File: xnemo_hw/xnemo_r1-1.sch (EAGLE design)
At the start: 36 parts, among them J1 MICRO_USB_B_RECEPT, J2 DM3D_MICRO_SD, J3 HEADER_2X5_0.05_SMD, J4 HEADER_2X5_0.05_THRU, J5 HEADER_2X5_0.05_THRU, U1 LTC3559, U2 L3GD20, U3 STM32F405RG, U5 HMC5883L, U6 ADXL345, X1 TXC_7A_XTAL

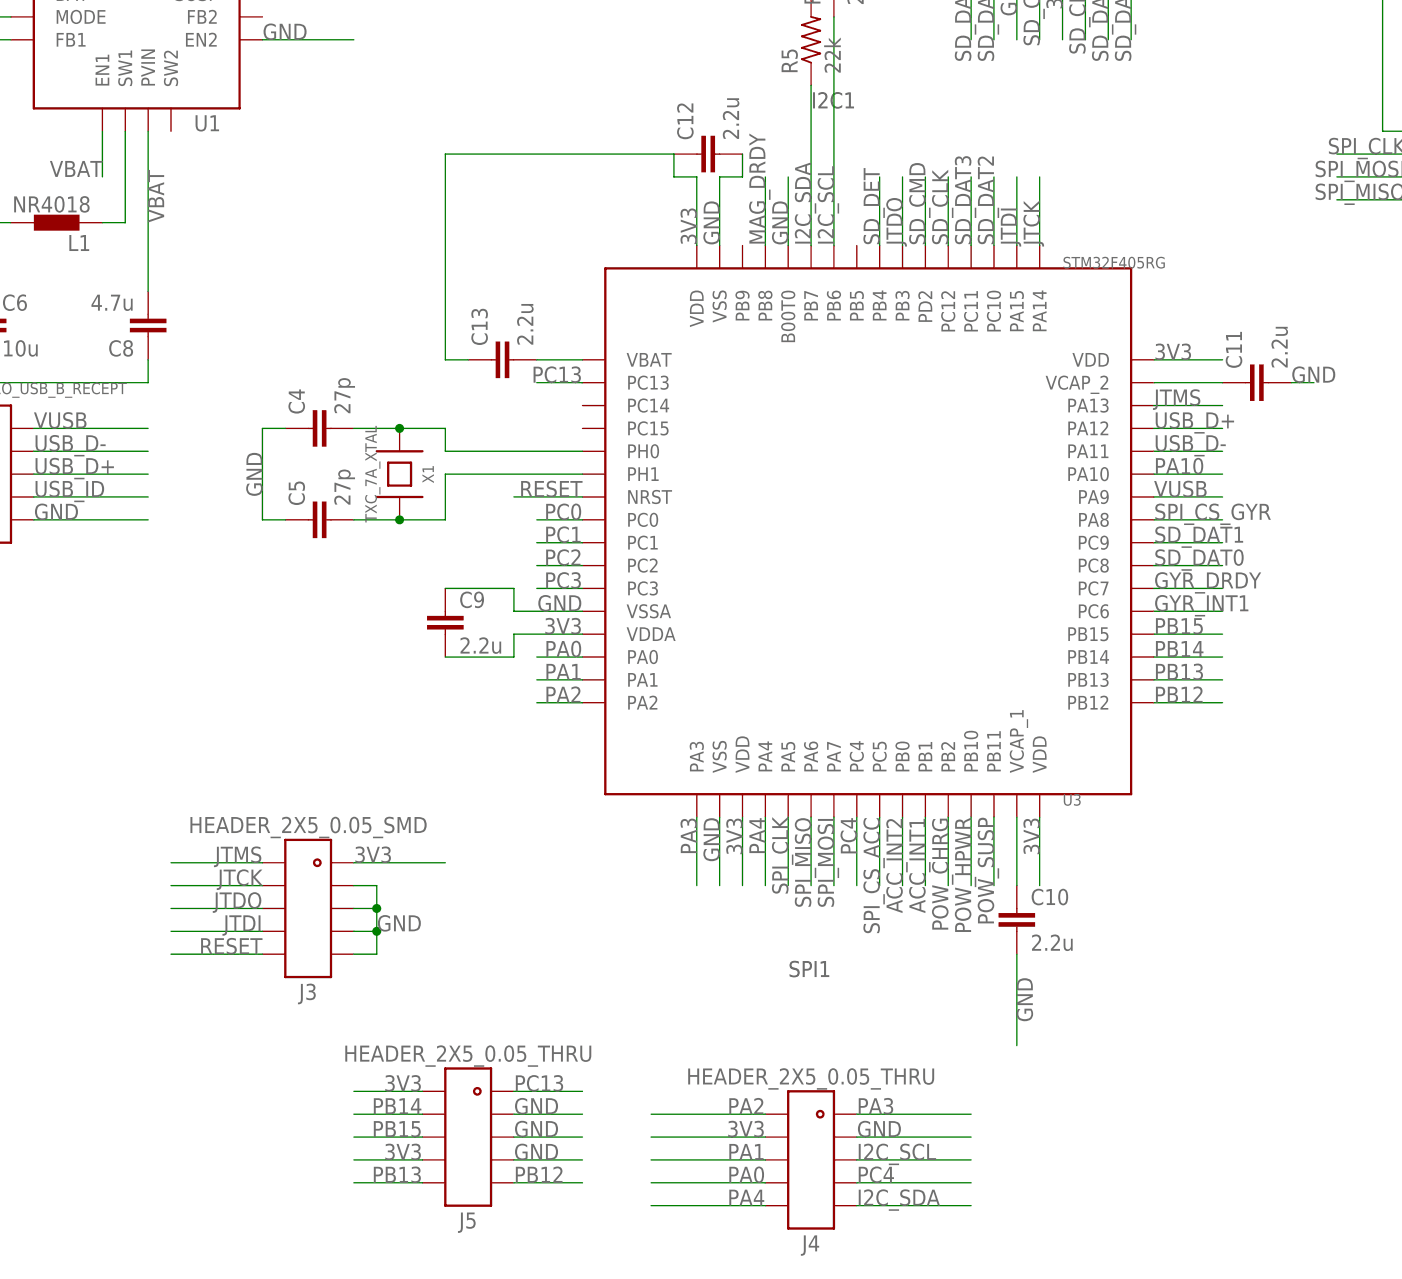
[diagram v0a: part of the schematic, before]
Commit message: Fixing up R1 schematic for R1A
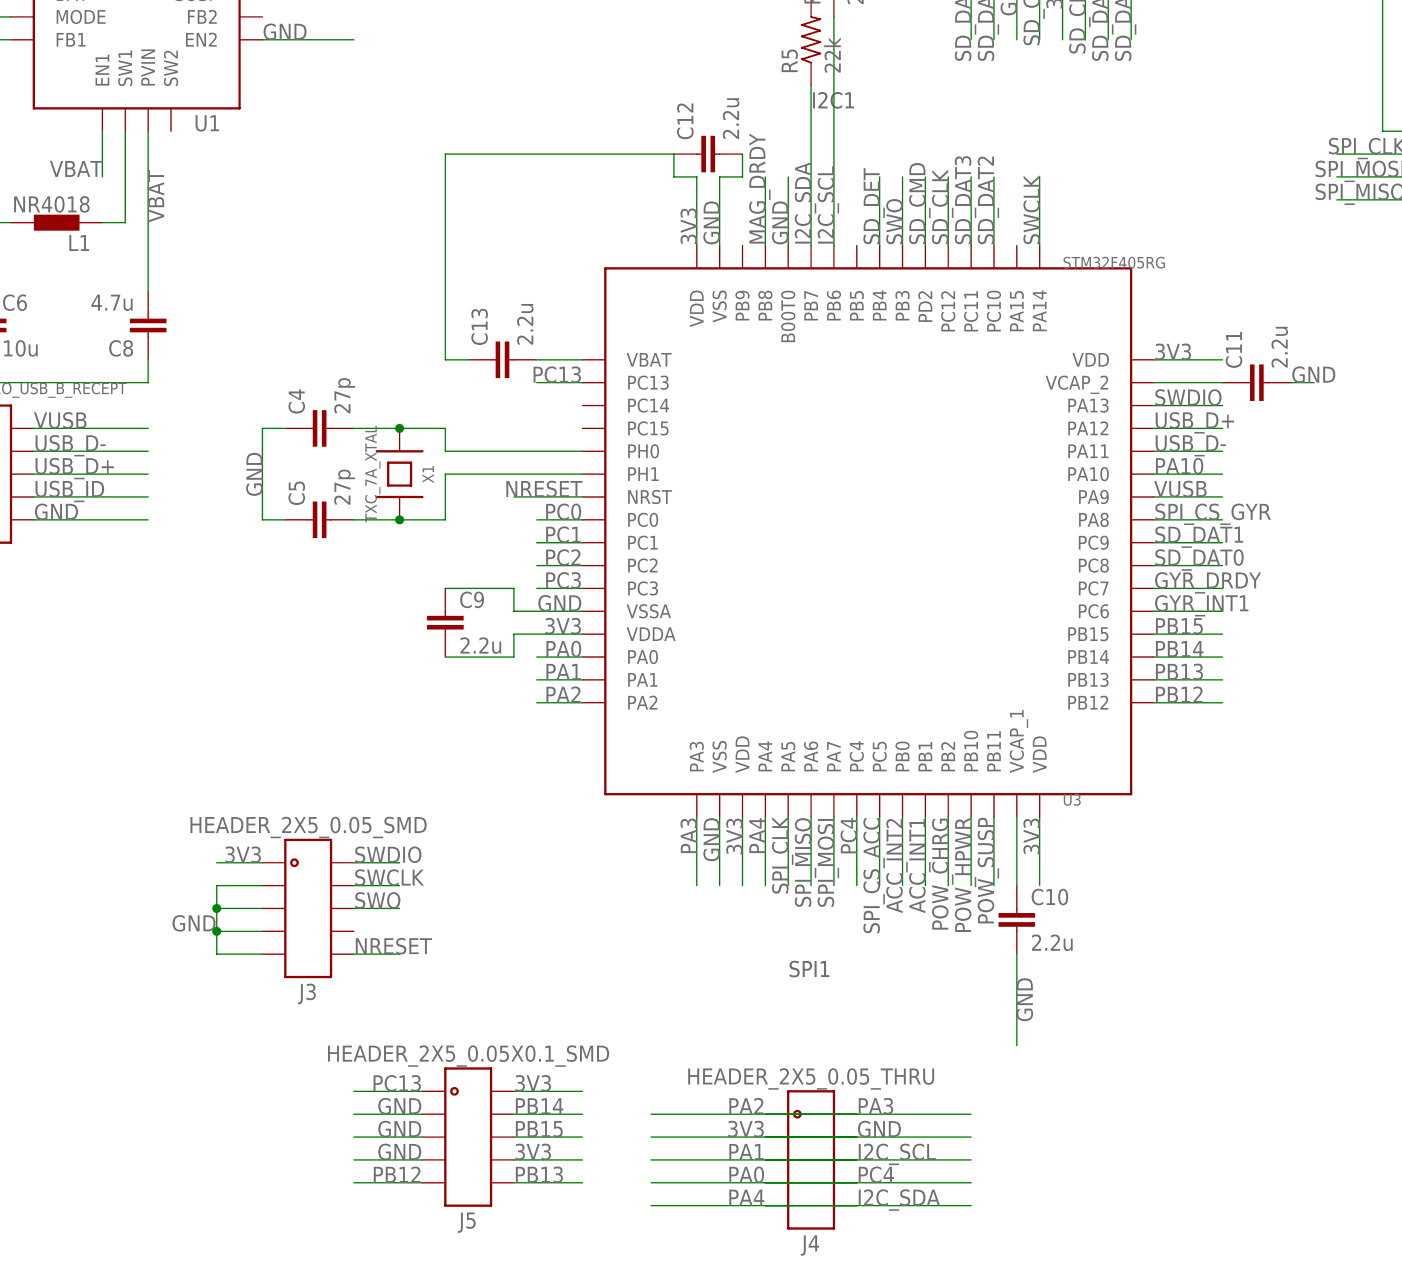
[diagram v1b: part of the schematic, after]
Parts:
- J5: value HEADER_2X5_0.05_THRU -> HEADER_2X5_0.05X0.1_SMD; device xnemo:HEADER_2X5_0.05_THRU -> xnemo:HEADER_2X5_0.05X0.1_SMD
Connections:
- net JTCK renamed SWCLK
- net JTDO renamed SWO
- net JTMS renamed SWDIO
- net RESET renamed NRESET
- removed net JTDI: J3.8, U3.PA15

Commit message: I don't remember
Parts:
- added C19: 100n, resistor:C-EUC0402
- added C20: 10u, resistor:C-EUC0805
- added LED1, LED2: (no value), led:LEDCHIPLED_0603
- added R4: (no value), xnemo:RESISTOR-0603
- added R7, R8: (no value), xnemo:RESISTOR-0402
- added SW1, SW2: ALPS_SKQG, xnemo:ALPS_SKQG
- added U4: LPS331AP, xnemo:LPS331AP
- C14: value 22p -> 10p
- J4: value HEADER_2X5_0.05_THRU -> HEADER_2X5_0.05X0.1_THRU; device xnemo:HEADER_2X5_0.05_THRU -> xnemo:HEADER_2X5_0.05X0.1_THRU
- J5: value HEADER_2X5_0.05X0.1_SMD -> HEADER_2X5_0.05X0.1_THRU; device xnemo:HEADER_2X5_0.05X0.1_SMD -> xnemo:HEADER_2X5_0.05X0.1_THRU
- R1, R2, R3, R5, R6: device resistor:R-US_R0402 -> xnemo:RESISTOR-0402
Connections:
- new net 3V3A: R4.P$2, U4.VCCA
- new net N$2: LED1.A, R7.P$2
- new net N$3: LED2.A, R8.P$2
- new net PC14: R7.P$1, U3.PC14
- new net PC15: R8.P$1, U3.PC15
- new net SPI_CS_PRS: U4.NCS
- new net USER_BTN: SW2.1@1, U3.PB5
- net 3V3: now also C19.2, C20.1, R1.P$1, R4.P$1, R5.P$1, R6.P$1, U4.VDD, U4.VDDIO; no longer R1.2, R5.2, R6.2
- net BUCK_FB1: now also R1.P$2, R2.P$1; no longer R1.1, R2.2
- net GND: now also C19.1, C20.2, LED1.C, LED2.C, R2.P$2, R3.P$2, SW1.2@2, SW2.2@2, U4.GND@1, U4.GND@2, U4.GND@3, U4.GND@4, U4.RES; no longer R2.1, R3.2
- net I2C_SCL: now also R6.P$2; no longer R6.1
- net I2C_SDA: now also R5.P$2; no longer R5.1
- net NRESET: now also SW1.1@2
- net POW_PROG: now also R3.P$1; no longer R3.1
- net SPI_CLK: now also U4.SCL
- net SPI_MISO: no longer U2.SDO, U6.SDO
- net SPI_MOSI: now also U4.SDI
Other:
- moved on the sheet: R1, R2, R3, R5, R6
